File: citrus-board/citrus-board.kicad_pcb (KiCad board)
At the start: 4 copper layers, 27 x 60 mm, 65 parts, among them J1 SHOU_HAN_USB_C_Receptacle_USB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, J2 Conn_01x02, J3 Conn_01x03_MountingPin, J4 0.5mm FPC, J5 Conn_01x13, J6 Conn_01x13, SW1 SW_Push, SW2 SW_Push, U1 BQ24074RGT, U2 TPS63000-Q1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

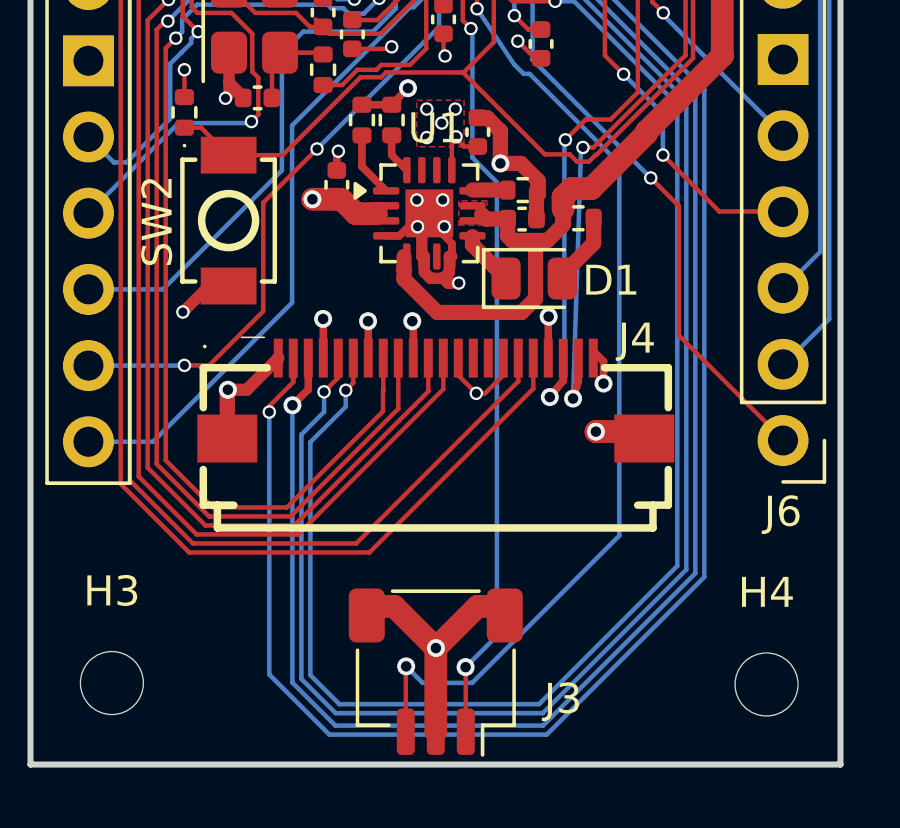
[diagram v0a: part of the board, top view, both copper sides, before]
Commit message: zine + rotate debug connector
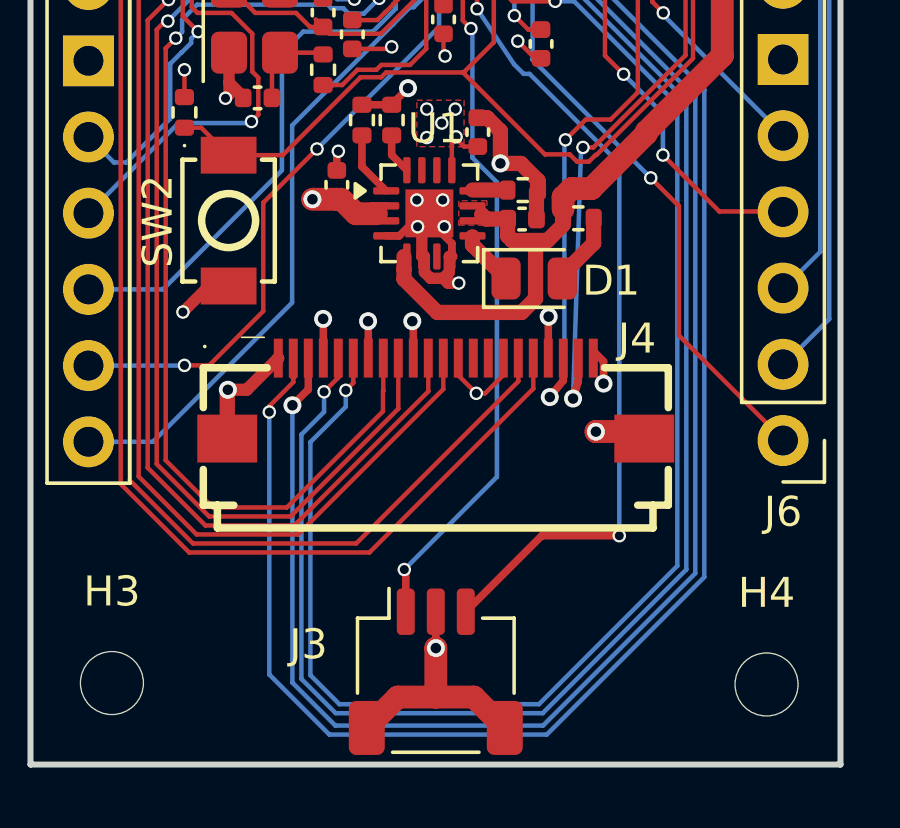
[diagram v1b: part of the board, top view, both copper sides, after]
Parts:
- turned J3 to 0 degrees
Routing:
- net /SWDIO: track 32.9 -> 27.5 mm
- net /SWCLK: track 26.8 -> 23.7 mm

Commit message: update fields + production export
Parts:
- C15, C16, C7: footprint Capacitor_SMD:C_0402_1005Metric -> Capacitor_SMD:C_0805_2012Metric
- C3: footprint Capacitor_SMD:C_0402_1005Metric -> Capacitor_SMD:C_0603_1608Metric
- moved R17 2.66 mm to (137.0, 57.1), turned to 90 degrees
- moved C15 2.33 mm to (136.6, 54.2), turned to 90 degrees
- moved C7 1.66 mm to (133.8, 50.8), turned to 0 degrees
- moved R4 1.32 mm to (142.4, 53.6)
- moved L1 1.01 mm to (139.8, 55.0)
- moved R5 0.81 mm to (144.6, 53.0)
- moved C16 0.78 mm to (134.2, 58.0)
- moved C3 0.63 mm to (144.8, 83.4)
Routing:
- net GNDPWR: track 9.32 -> 11.7 mm
- net Net-(U2-L2): track 4.50 -> 6.38 mm
- net Net-(U2-L1): track 4.39 -> 6.24 mm
- net +3V3: track 37.8 -> 39.4 mm, vias 18 -> 19
- net GND: track 69.9 -> 71.4 mm, vias 38 -> 37
- net Net-(J1-CC2): track 1.22 -> 2.56 mm
- net /QSPI_SS: track 31.7 -> 31.0 mm
- net /BC_OUT: track 72.2 -> 72.8 mm, vias 1 -> 2
